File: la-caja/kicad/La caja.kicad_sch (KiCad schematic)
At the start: 0 parts

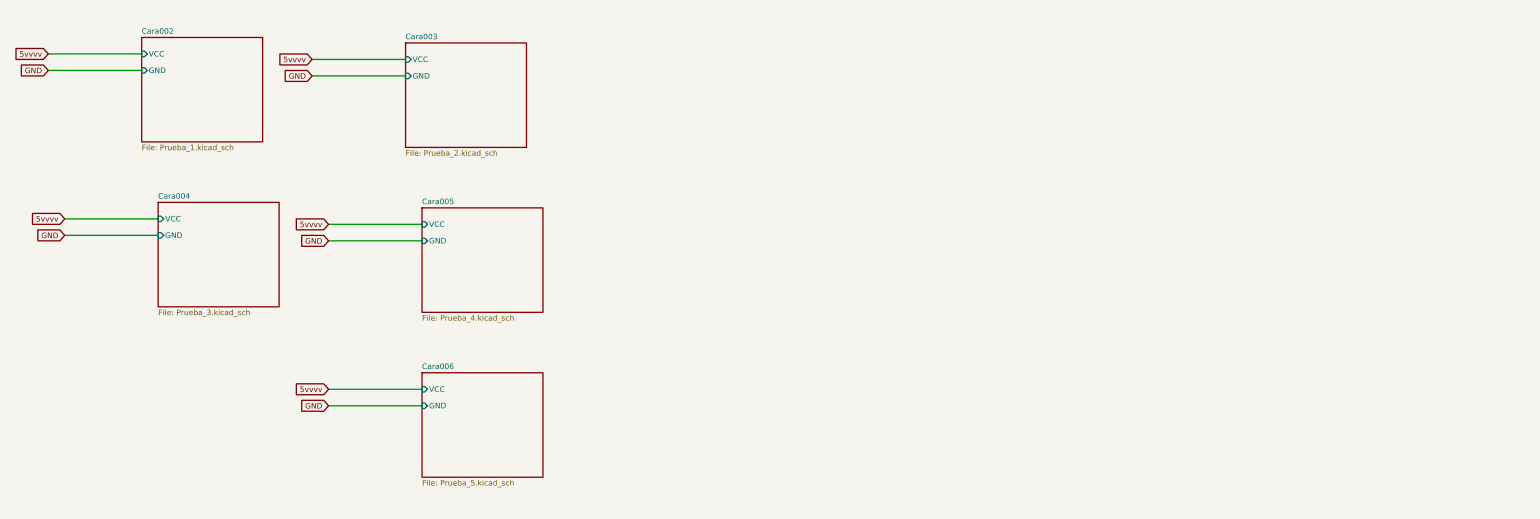
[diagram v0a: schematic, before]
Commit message: Esquematico actualizado, nuevo símbolo para numpad
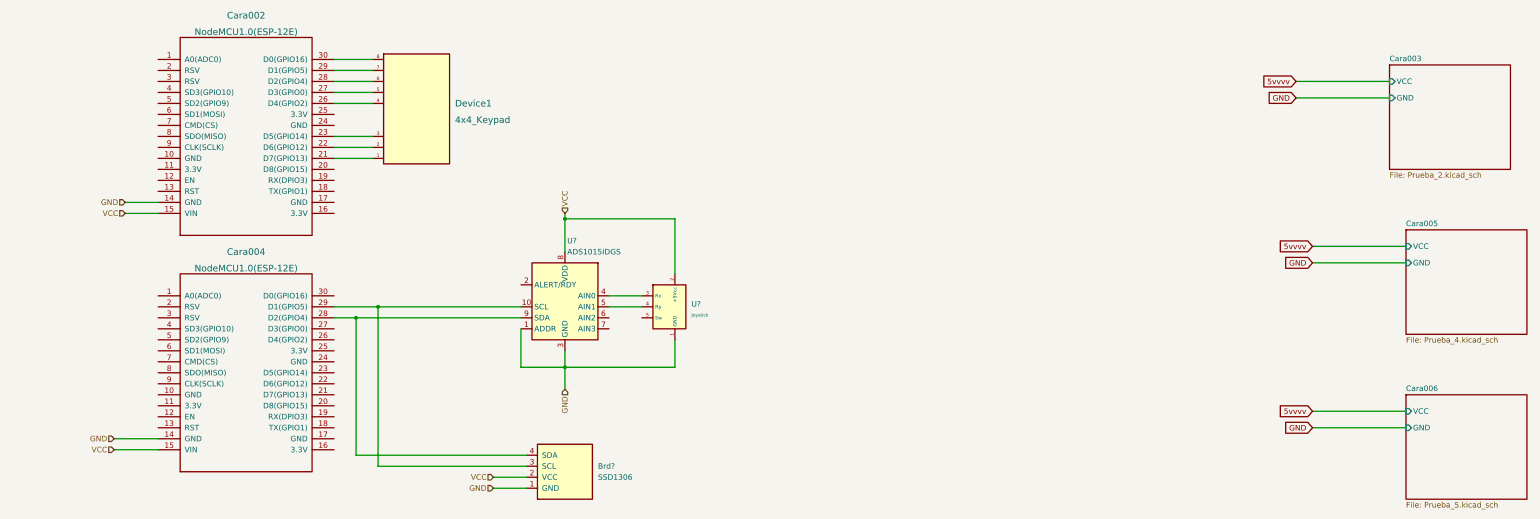
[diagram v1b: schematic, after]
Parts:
- added Brd?: SSD1306, symbol LCD:SSD1306
- added Cara002, Cara004: NodeMCU1.0(ESP-12E), symbol ESP8266:NodeMCU1.0(ESP-12E)
- added Device1: 4x4_Keypad, symbol LaCaja_simbolos:4x4_Keypad
- added U?: Joystick, symbol LaCaja_simbolos:Joystick
- added U?: ADS1015IDGS, Package_SO:TSSOP-10_3x3mm_P0.5mm, symbol Analog_ADC:ADS1015IDGS
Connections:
- net GND: now also Brd?.1 (GND), Cara002.14 (GND), Cara004.14 (GND), U?.1 (ADDR), U?.1 (GND), U?.3 (GND)
- new net: U?.3 (Rx), U?.4 (AIN0)
- new net: U?.4 (Ry), U?.5 (AIN1)
- new net: Cara002.21 (D7(GPIO13)), Device1.1
- new net: Cara002.22 (D6(GPIO12)), Device1.2
- new net: Cara002.23 (D5(GPIO14)), Device1.3
- new net: Cara002.26 (D4(GPIO2)), Device1.4
- new net: Cara002.27 (D3(GPIO0)), Device1.5
- new net: Cara002.28 (D2(GPIO4)), Device1.6
- new net: Cara002.29 (D1(GPIO5)), Device1.7
- new net: Cara002.30 (D0(GPIO16)), Device1.8
- new net: Brd?.3 (SCL), Cara004.29 (D1(GPIO5)), U?.10 (SCL)
- new net: Brd?.4 (SDA), Cara004.28 (D2(GPIO4)), U?.9 (SDA)
- new net VCC: Brd?.2 (VCC), Cara002.15 (VIN), Cara004.15 (VIN), U?.2 (+5Vcc), U?.8 (VDD)
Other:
- removed sheet Cara002
- removed sheet Cara004

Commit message: Cambios en KiCAD
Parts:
- added BZ?: Buzzer, symbol Device:Buzzer
- added Cara005, Cara006, PRUEBA?: NodeMCU1.0(ESP-12E), symbol ESP8266:NodeMCU1.0(ESP-12E)
- added D? (x4): LED, symbol Device:LED
- added R1, R2, R3, R4, R5: 10k, symbol Device:R
- added R? (x8): R, symbol Device:R
- added SW1, SW2, SW? (x4): SW_Push, symbol Switch:SW_Push
- added SW1, SW2, SW3, SW4, SW5: SW_DPDT_x2, symbol Switch:SW_DPDT_x2
- added U1: LDR, symbol LaCaja_simbolos:LDR
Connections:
- net GND: now also Cara005.14 (GND), Cara006.14 (GND), PRUEBA?.14 (GND)
- net VCC: now also Cara005.15 (VIN), Cara006.15 (VIN), PRUEBA?.15 (VIN)
- new net: Cara005.26 (D4(GPIO2)), R3.1, SW3.1 (A)
- new net: Cara005.11 (3.3V), SW1.2 (B), SW2.2 (B), SW3.2 (B), SW4.2 (B), SW5.2 (B)
- new net: Cara005.28 (D2(GPIO4)), R1.1, SW1.1 (A)
- new net: Cara005.24 (GND), R1.2, R2.2, R3.2, R4.2, R5.2
- new net: Cara005.27 (D3(GPIO0)), R2.1, SW2.1 (A)
- new net: PRUEBA?.27 (D3(GPIO0)), R?.1
- new net: D?.2 (A), R?.2 (x4)
- new net: Cara006.25 (3.3V), SW2.1
- new net: Cara006.20 (D8(GPIO15)), SW2.2
- new net: Cara005.22 (D6(GPIO12)), R5.1, SW5.1 (A)
- new net: Cara005.23 (D5(GPIO14)), R4.1, SW4.1 (A)
- new net: Cara005.25 (3.3V), SW1.1
- new net: Cara005.29 (D1(GPIO5)), SW1.2
- new net: Cara006.1 (A0(ADC0)), U1.1 (Output)
- new net: Cara006.10 (GND), U1.3 (GND)
- new net: Cara006.11 (3.3V), U1.2 (VCC)
- new net: PRUEBA?.29 (D1(GPIO5)), R?.1
- new net: BZ?.1 (-), PRUEBA?.25 (3.3V)
- new net: BZ?.2 (+), PRUEBA?.24 (GND)
- new net: PRUEBA?.28 (D2(GPIO4)), R?.1
- new net: PRUEBA?.30 (D0(GPIO16)), R?.1
- no-connect marks 0 -> 6
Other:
- removed sheet Cara003
- removed sheet Cara005
- removed sheet Cara006
- company: Proyecto la Caja ->    LaCaja
- title: Testing de esquematicos -> Hardware de las caras
- moved on the sheet: Brd?, Cara002, Cara004, Device1, U?

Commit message: Esquematico la Caja
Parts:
- removed SW? (x4): SW_Push, symbol Switch:SW_Push
- added U? (x4): sw_4_pin, symbol LaCaja_simbolos:sw_4_pin
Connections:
- net at R?.1: no longer PRUEBA?.27 (D3(GPIO0))
- net at R?.1: no longer PRUEBA?.29 (D1(GPIO5))
- net at BZ?.1 (-): now also PRUEBA?.22 (D6(GPIO12)); no longer PRUEBA?.25 (3.3V)
- net at PRUEBA?.28 (D2(GPIO4)): no longer R?.1
- net at PRUEBA?.30 (D0(GPIO16)): no longer R?.1
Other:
- moved on the sheet: BZ?, D?, R?

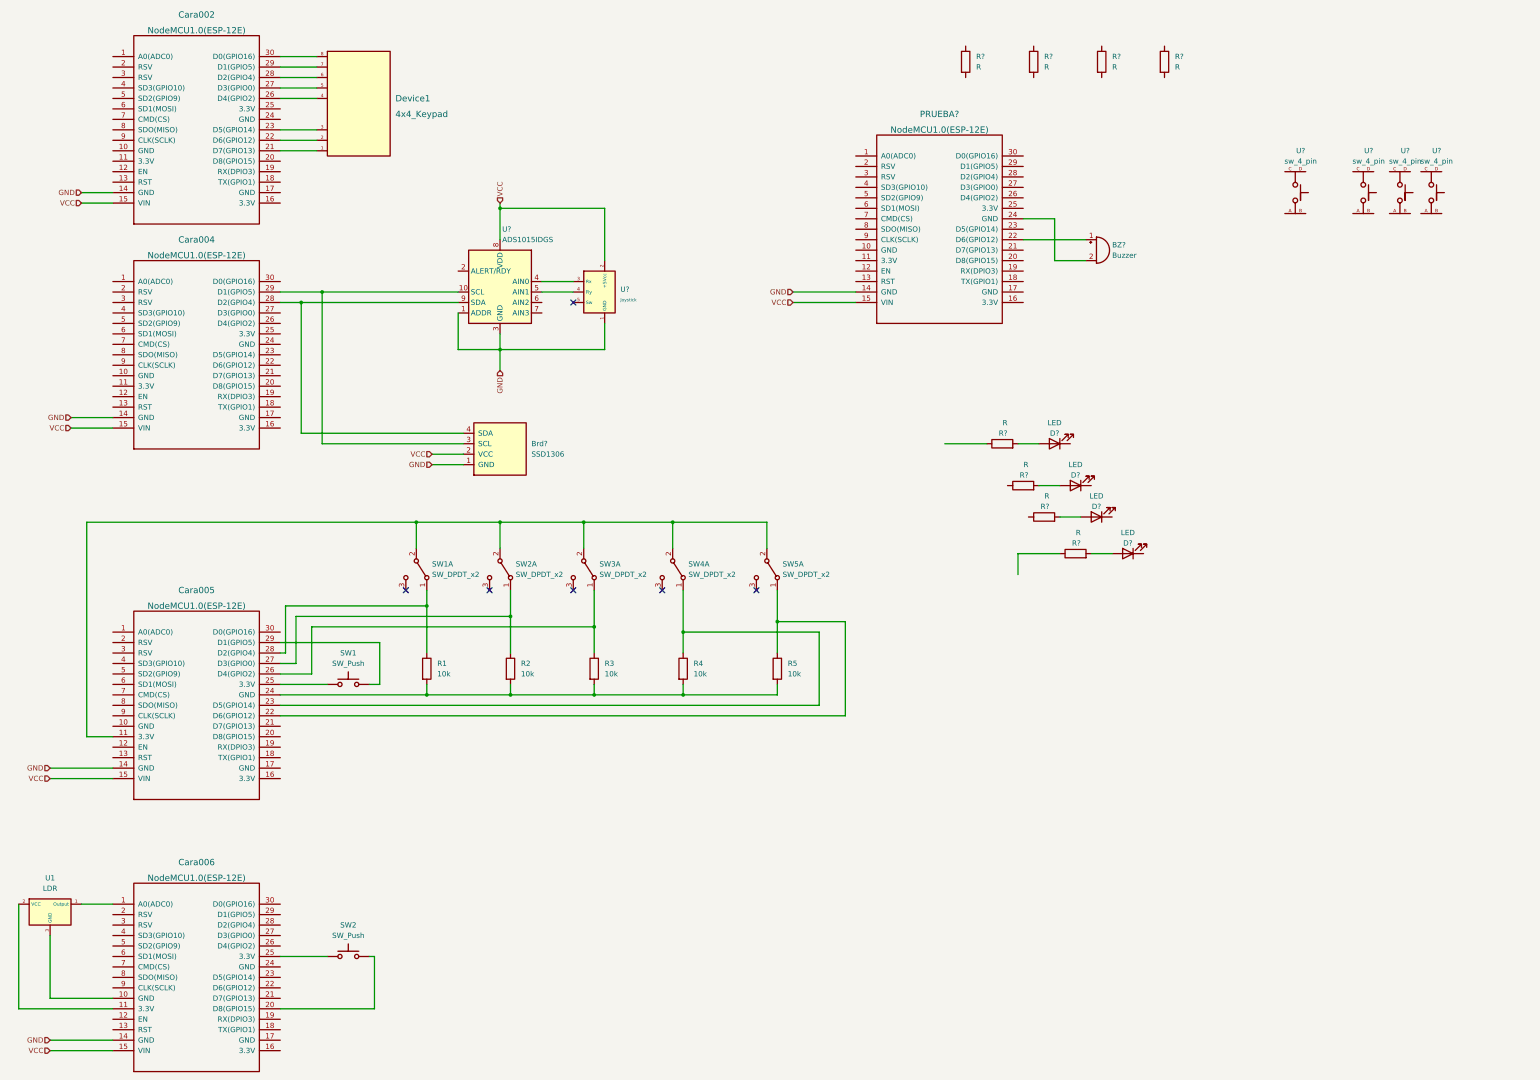
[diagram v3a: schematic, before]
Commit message: Esquematico en kicad terminado
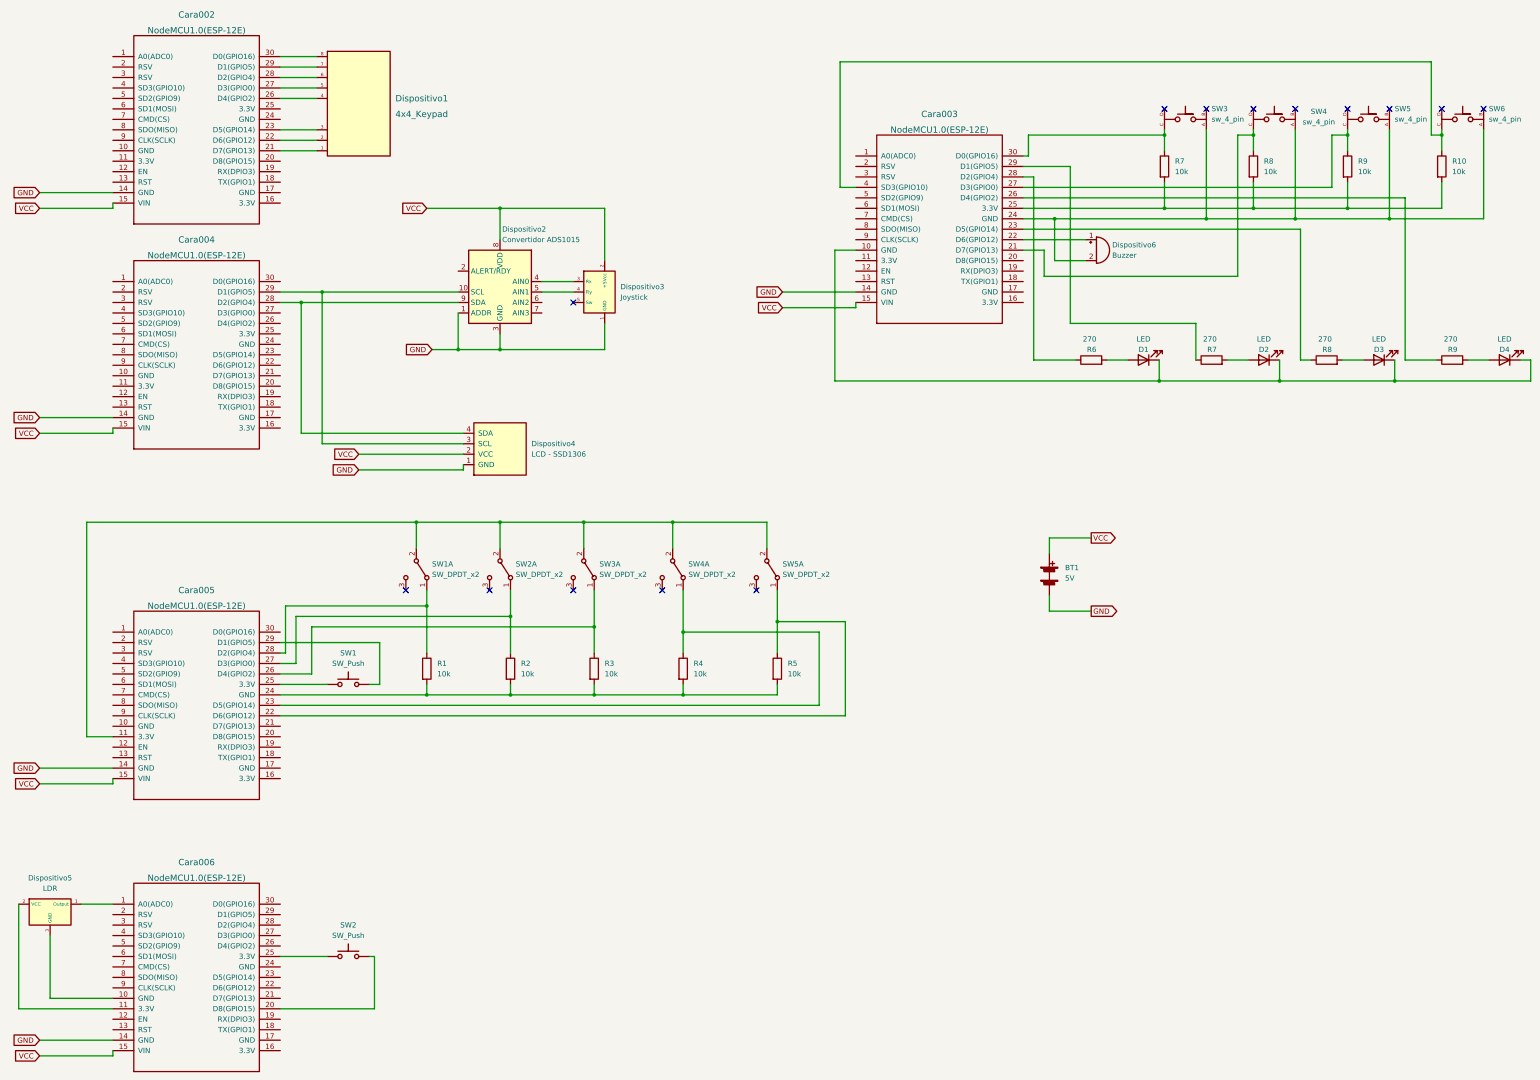
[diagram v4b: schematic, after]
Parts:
- added BT1: 5V, symbol Device:Battery
- Dispositivo2: renamed from U?; value ADS1015IDGS -> Convertidor ADS1015
- Dispositivo4: renamed from Brd?; value SSD1306 -> LCD - SSD1306
- R10, R7, R8, R9: renamed from R?; value R -> 10k
- R6, R7, R8, R9: renamed from R?; value R -> 270
- gave numbers to parts that had none: 11
- renumbered Device1 to Dispositivo1, U1 to Dispositivo5
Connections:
- net GND: now also BT1.2 (-)
- net VCC: now also BT1.1 (+)
- net at R9.1: now also Cara003.26 (D4(GPIO2))
- net at D1.1 (K): now also Cara003.10 (GND), D2.1 (K), D3.1 (K), D4.1 (K)
- net at R7.1: now also Cara003.30 (D0(GPIO16)), SW3.C
- net at R7.2: now also Cara003.25 (3.3V), R10.2, R8.2, R9.2
- net at R7.1: now also Cara003.29 (D1(GPIO5))
- net at R10.1: now also Cara003.4 (SD3(GPIO10)), SW6.C
- net at R9.1: now also Cara003.27 (D3(GPIO0)), SW5.C
- net at Cara003.24 (GND), Dispositivo6.2 (+): now also SW3.A, SW4.A, SW5.A, SW6.A
- net at SW4.C: now also Cara003.21 (D7(GPIO13)), R8.1
- net at Cara003.23 (D5(GPIO14)): now also R8.1
- net at Cara003.28 (D2(GPIO4)): now also R6.1
- no-connect marks 6 -> 14
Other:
- moved on the sheet: D1, D2, D3, D4, R10, R6, R7, R8, R9, SW3, SW4, SW5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
